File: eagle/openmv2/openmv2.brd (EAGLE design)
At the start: 43.2 x 54.6 mm, 82 parts, among them J3 CON_HEADER_1X03, J4 CON_HEADER_1X03, Q1 MOSFET, U1 TPS2114APW, U10 IS42S16800E, U2 USD-47571, U3 BEAD, U4 TPS768, U5 BEAD, U6 BEAD, U7 STM32F429, U8 VREG_25, U9 OV2640, X1 USB-MICROB

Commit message: Fix SDRAM part-no
* Issue #29
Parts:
- U10: value IS42S16800E -> IS42S81600E-7TL
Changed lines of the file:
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@@
 <layer number="21" name="tPlace" color="7" fill="1" visible="yes" active="yes"/>
 <layer number="22" name="bPlace" color="7" fill="1" visible="yes" active="yes"/>
-<layer number="23" name="tOrigins" color="15" fill="1" visible="no" active="yes"/>
-<layer number="24" name="bOrigins" color="15" fill="1" visible="no" active="yes"/>
+<layer number="23" name="tOrigins" color="15" fill="1" visible="yes" active="yes"/>
+<layer number="24" name="bOrigins" color="15" fill="1" visible="yes" active="yes"/>
 <layer number="25" name="tNames" color="7" fill="1" visible="no" active="yes"/>
 <layer number="26" name="bNames" color="7" fill="1" visible="no" active="yes"/>
@@
 <attribute name="VALUE" x="18.6055" y="32.131" size="0.4064" layer="27"/>
 </element>
-<element name="U10" library="mux" package="TSOPII-54" value="IS42S16800E" x="21.59" y="21.717" smashed="yes" rot="MR270">
+<element name="U10" library="mux" package="TSOPII-54" value="IS42S81600E-7TL" x="21.59" y="21.717" smashed="yes" rot="MR270">
 <attribute name="NAME" x="26.5696" y="9.5388" size="0.6096" layer="26" font="vector" ratio="20" rot="MR0"/>
 <attribute name="VALUE" x="21.8686" y="30.1956" size="1.27" layer="28" rot="MR270"/>

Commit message: Rename Eagle files
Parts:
- removed C12, C21: 100uF, sfe:EIA3216
- removed C25, C26, C27, C28, C29, C31, C32, C35, C36, C37, C43: 0.1uF, sfe:0402-CAP
- removed C30: 10uF, sfe:0805
- removed C33, C34: 2.2uF, sfe:0402-CAP
- removed C38: 100uF, sfe:EIA3528
- removed H1, H8: MOUNT-PAD-ROUND2.8, holes:2,8-PAD
- removed R12: 1K, sfe:0402-RES
- removed R4: 10ohm, iofault:0402-RES
- removed RN2, RN8: (no value), resistor-dil:CAT16
- removed U$1: LENSMOUNT, omnivision:LENSMOUNT
- removed U$14, U$15, U$16, U$17, U$19, U$20: FIDUCIAL, adafruit:FIDUCIAL_1MM
- removed U10: IS42S81600E-7TL, mux:TSOPII-54
- removed U5: BEAD, heka:0402-CAP
- removed X1: USB-MICROB, sfe:USB-MICROB
- added C48, C49: 2.2uF, sfe:0603-CAP
- added D1: BAT54C, diode:SOT23
- added JP3, JP4: (no value), pinhead:1X08
- added JP5, JP6, JP7, JP8: FIDUCIAL1X2, sfe:FIDUCIAL-1X2
- added R2: 10k, sfe:0603-RES
- added U$3: (no value), openmv:OMV-LOGO
- added U12: STM32F427-LQFP100, mux:LQFP100
- added X2: USB-MICROB, sfe:USB-MICROB
- C1: value 0.1uF -> 22uF; device sfe:0402-CAP -> sfe:0805
- C10, C13, C14, C15, C16, C17, C18, C19, C20, C4, C5, C6, C7, C8, C9: device sfe:0402-CAP -> sfe:0603-CAP
- C11: value 100uF -> 22uF; device sfe:EIA3528 -> sfe:0805
- C2: value 0.1uF -> 4.7uF; device sfe:0402-CAP -> sfe:0603-CAP
- C23, C24: value 10uF -> 4.7uF; device sfe:0402-CAP -> sfe:0603-CAP
- C3: device sfe:EIA3216 -> sfe:1206
- C40, C41: value 18pF -> 12pF; device sfe:0402-CAP -> sfe:0603-CAP
- JP1, JP2: value (none) -> FIDUCIAL1X2; device pinhead:1X10 -> sfe:FIDUCIAL-1X2
- LOGO1: value OSHW_LOGO_FILLX0200-NT -> OSHW_LOGO_FILLX0150-NT; device iofault:OSHW_FILLX200_NOTEXT -> iofault:OSHW_FILLX150_NOTEXT
- R1: value 10K -> 10ohm; device sfe:0402-RES -> sfe:0603-RES
- R5: device sfe:0402-RES -> sfe:0603-RES
- RN4: value (none) -> 220R; device resistor-dil:CAT16 -> resistor-dil:EXBV8V
- RN5, RN6: value (none) -> 10K; device resistor-dil:CAT16 -> resistor-dil:EXBV8V
- RN7: value (none) -> 10K
- U1: value TPS2114APW -> LENSMOUNT20MM; device mux:TSSOP8 -> omnivision:LENSMOUNT-20MM
- U3, U6: value BEAD -> (none); device heka:0402-CAP -> sfe:0603
- U4: value TPS768 -> BD33IA; device mux:SOIC8 -> mux:HTSOP-J8
- U7: value STM32F429 -> (none); device stm32:LQFP144 -> sfe:0603
- U8: value VREG_25 -> VREG_28
- Y1: device mux:CRYSTAL3.2X2.5 -> mux:CRYSTAL-2.5X2.0
- moved C3 44.8 mm to (6.22, 2.92), turned to 270 degrees
- moved H2 37.4 mm to (3.30, 41.1)
- moved JP2 34.1 mm to (7.87, 6.10), flipped to the bottom, turned to 0 degrees
- moved U1 32.3 mm to (17.8, 36.0), turned to 0 degrees
- moved H6 30.1 mm to (32.3, 41.1)
- moved C7 27.5 mm to (12.4, 6.48), turned to 180 degrees
- moved C6 25.7 mm to (9.91, 25.0)
- moved C11 23.6 mm to (8.13, 25.0), turned to 270 degrees
- moved R1 23.5 mm to (6.22, 25.0), flipped to the top
- moved C2 23.0 mm to (16.5, 3.30)
- moved C14 22.7 mm to (8.26, 13.7), turned to 270 degrees
- moved R5 19.0 mm to (2.03, 22.2), flipped to the top, turned to 180 degrees
- moved C1 18.9 mm to (27.2, 26.8), turned to 270 degrees
- moved LOGO1 16.7 mm to (26.9, 11.4), flipped to the top
- moved LED3 16.5 mm to (2.41, 35.6), turned to 270 degrees
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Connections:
- removed net ADC12_IN14: JP1.8, U7.44
- removed net ADC12_IN15: JP1.7, U7.45
- removed net ADC12_IN5: U7.41
- removed net DCMI_SCL: RN7.2, U7.69, U9.C2
- removed net DCMI_SDA: RN7.1, U7.70, U9.C1
- removed net DRAM_A0: U10.23, U7.10
- removed net DRAM_A1: U10.24, U7.11
- removed net DRAM_A10: U10.22, U7.56
- removed net DRAM_A11: U10.35, U7.57
- removed net DRAM_A2: U10.25, U7.12
- removed net DRAM_A3: U10.26, U7.13
- removed net DRAM_A4: U10.29, U7.14
- removed net DRAM_A5: U10.30, U7.15
- removed net DRAM_A6: U10.31, U7.50
- removed net DRAM_A7: U10.32, U7.53
- removed net DRAM_A8: U10.33, U7.54
- removed net DRAM_A9: U10.34, U7.55
- removed net DRAM_BA0: U10.20, U7.89
- removed net DRAM_BA1: U10.21, U7.90
- removed net DRAM_CAS: U10.17, U7.132
- removed net DRAM_CLK: U10.38, U7.93
- removed net DRAM_CLKE: U10.37, U7.29
- removed net DRAM_CS: R1.2, U10.19, U7.28
- removed net DRAM_D0: U10.2, U7.85
- removed net DRAM_D1: U10.5, U7.86
- removed net DRAM_D2: U10.8, U7.114
- removed net DRAM_D3: U10.11, U7.115
- removed net DRAM_D4: U10.44, U7.58
- removed net DRAM_D5: U10.47, U7.59
- removed net DRAM_D6: U10.50, U7.60
- removed net DRAM_D7: U10.53, U7.63
- removed net DRAM_DQM: U10.39, U7.141
- removed net DRAM_RAS: U10.18, U7.49
- removed net DRAM_WE: U10.16, U7.26
- removed net FS_DN: U7.103, X1.D-
- removed net N$15: U7.128
- removed net N$17: U7.92
- removed net N$18: U7.18
- removed net N$19: U7.91
- removed net N$20: JP1.1, RN8.1
- removed net N$21: JP1.2, RN8.2
- removed net N$22: U5.1, X1.VBUS
- removed net N$23: JP1.3, RN8.3
- removed net N$24: JP1.4, RN8.4
- removed net N$25: U7.122
- removed net N$26: R12.2, U1.4
- removed net N$27: U7.19
- removed net N$28: U7.20
- removed net SPI4_MISO: RN8.6, U7.4
- removed net SPI4_MOSI: RN8.5, U7.5
- removed net SPI4_NSS: RN8.7, U7.2
- removed net SPI4_SCK: RN8.8, U7.1
- removed net TIM12_CH1: U7.75
- removed net TIM12_CH2: U7.76
- removed net USART2_RX: JP1.6, U7.37
- removed net USART2_TX: JP1.5, U7.36
- removed net USART3_RX: JP2.7, U7.78
- removed net USART3_TX: JP2.8, U7.77
- removed net VBAT: J3.2, J4.2, JP2.9, U1.6
- new net DAC: JP4.7, U12.30
- new net EXPST: U12.55, U9.A2
- new net FREX: U12.56, U9.B2
- new net FS_DM: U12.70, X2.D-
- new net I2C1_SCL: RN7.2, U12.95, U9.C2
- new net I2C1_SDA: RN7.1, U12.96, U9.C1
- new net I2C2_SCL: JP4.5, U12.47
- new net I2C2_SDA: JP4.6, U12.48
- new net RAW: D1.1, J3.2, J4.2, JP3.7
- new net SPI2_MISO: JP4.2, U12.53
- new net SPI2_MOSI: JP4.1, U12.54
- new net SPI2_NSS: JP4.4, U12.51
- new net SPI2_SCLK: JP4.3, U12.52
- new net STROBE: U12.84, U9.A6
- net BOOT0: now also JP3.3, RN5.8, U12.94; no longer JP2.3, RN2.6, U7.138
- net DCMI_CLK: now also U12.67; no longer U7.100
- net DCMI_D0: now also U12.63; no longer U7.96
- net DCMI_D1: now also U12.64; no longer U7.97
- net DCMI_D2: now also U12.97; no longer U7.125
- net DCMI_D3: now also U12.98; no longer U7.126
- net DCMI_D4: now also U12.3; no longer U7.3
- net DCMI_D5: now also U12.92; no longer U7.117
- net DCMI_D6: now also U12.4; no longer U7.139
- net DCMI_D7: now also U12.5; no longer U7.140
- net DCMI_HSYNC: now also U12.29; no longer U7.40
- net DCMI_PCLK: now also U12.31; no longer U7.42
- net DCMI_PWDN: now also U12.91; no longer U7.102
- net DCMI_RST: now also U12.69; no longer U7.110
- net DCMI_VSYNC: now also U12.93; no longer U7.137
- net FS_DP: now also U12.71, X2.D+; no longer U7.104, X1.D+
- net GND: now also C11.1, C3.2, C48.2, C49.2, JP3.8, R2.1, RN5.1, U12.10, U12.20, U12.27, U12.37, U12.74, U12.99, U4.3, U4.P$1, X2.GND; no longer C11.C, C12.C, C21.C, C25.2, C26.2, C27.2, C28.1, C29.2, C3.C, C30.2, C31.2, C32.2, C33.2, C34.2, C35.2, C36.2, C37.2, C38.C, C43.2, H1.B2,8, H2.B2,8, H6.B2,8, H8.B2,8, JP1.10, JP2.10, R12.1, RN2.1, RN2.3, U$1.P$1, U$1.P$2, U1.3, U1.5, U10.12, U10.28, U10.41, U10.46, U10.52, U10.54, U10.6, U4.1, U4.2, U7.107, U7.120, U7.130, U7.16, U7.31, U7.38, U7.48, U7.51, U7.61, U7.83, U7.94, U9.A2, U9.B2, X1.GND
- net LED_B: now also U12.16; no longer U7.135
- net LED_G: now also U12.17; no longer U7.136
- net LED_IR: now also U12.1; no longer U7.133
- net LED_R: now also U12.15; no longer U7.134
- net N$10: now also R1.2; no longer R4.1
- net N$12: now also C4.1, C5.1, U12.21, U12.22, U3.1; no longer U7.127
- net N$14: now also R1.1; no longer R4.2
- net N$2: now also U12.13; no longer U7.23
- net N$4: now also U12.12; no longer U7.24
- net N$5: now also R2.2
- net N$7: now also U7.1, X2.VBUS; no longer C4.1, C5.1, U3.1, U7.32, U7.33
- net NRST: now also JP3.4, RN5.7, U12.14; no longer JP2.4, RN2.5, U7.25
- net SDIO_CLK: now also U12.80; no longer U7.113
- net SDIO_CMD: now also U12.83; no longer U7.116
- net SDIO_D0: now also RN5.6, U12.65; no longer RN5.7, U7.98
- net SDIO_D1: now also U12.66; no longer U7.99
- net SDIO_D2: now also U12.78; no longer U7.111
- net SDIO_D3: now also U12.79; no longer U7.112
- net SD_CD: now also U12.77; no longer U7.124
- net SWCLK: now also JP3.1, U12.76; no longer JP2.1, RN2.8, U7.109
- net SWDIO: now also JP3.2, U12.72; no longer JP2.2, RN2.7, U7.105
- net TIM4_CH1: now also JP3.6, U12.59; no longer JP2.6, U7.81
- net TIM4_CH2: now also JP3.5, U12.60; no longer JP2.5, U7.82
- net VBUS: now also D1.2, U12.68, U7.2; no longer C43.1, U1.8, U5.2, U7.101
- net VCAP1: now also C49.1, U12.49; no longer C34.1, U7.71
- net VCAP2: now also C48.1, U12.73; no longer C33.1, U7.106
- net VCC: now also C11.2, C3.1, JP4.8, U12.100, U12.11, U12.19, U12.28, U12.50, U12.6, U12.75, U4.1, U4.2; no longer C12.A, C2.1, C21.A, C25.1, C26.1, C27.1, C28.2, C29.1, C3.A, C30.1, C31.1, C32.1, C35.1, C36.1, C37.1, C38.A, JP1.9, R1.1, RN2.2, RN2.4, RN5.1, U10.1, U10.14, U10.27, U10.3, U10.43, U10.49, U10.9, U4.5, U4.6, U7.108, U7.121, U7.131, U7.143, U7.144, U7.17, U7.30, U7.39, U7.52, U7.6, U7.62, U7.72, U7.84, U7.95
- net VIN: now also C2.1, D1.3, U4.5, U4.8; no longer C11.A, U1.7, U4.3, U4.4
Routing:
- net VCC: track 102.3 -> 26.3 mm, vias 32 -> 33
- net GND: track 123.5 -> 53.8 mm, vias 319 -> 61
- net DCMI_SCL: track 46.4 -> 0.00 mm, vias 4 -> 0
- net DCMI_SDA: track 43.5 -> 0.00 mm, vias 4 -> 0
- net EXPST: track 0.00 -> 39.3 mm, vias 0 -> 2
- net FREX: track 0.00 -> 37.3 mm, vias 0 -> 2
- net SPI2_SCLK: track 0.00 -> 30.5 mm
- net VBAT: track 30.2 -> 0.00 mm, vias 1 -> 0
- net SPI2_MOSI: track 0.00 -> 30.0 mm, vias 0 -> 1
- net SPI2_NSS: track 0.00 -> 28.8 mm
- net SPI2_MISO: track 0.00 -> 28.4 mm, vias 0 -> 1
- net FS_DN: track 26.3 -> 0.00 mm
- net DRAM_D7: track 25.8 -> 0.00 mm, vias 1 -> 0
- net I2C2_SDA: track 0.00 -> 25.7 mm, vias 0 -> 1
- net RAW: track 0.00 -> 24.1 mm, vias 0 -> 4
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- added copper zone on layer 1, net N$12
- added copper zone on layer 1, net N$7
- added copper zone on layer 1, net RAW
- added copper zone on layer 16, net RAW
- added copper zone on layer 1, net VBUS
- added copper zone on layer 1, net VCC
- added copper zone on layer 1, net VIN
- removed copper zone on layer 16, net GND
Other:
- board size 43.2 x 54.6 mm -> 35.6 x 44.5 mm
- board text added: "DAC"
- board text added: "MISO"
- board text added: "MOSI"
- board text added: "VCC"
- board text added: "VOUT"
- board text removed: "3.3v"
- board text removed: "ADC1"
- board text removed: "ADC2"
- board text removed: "OpenMV2 R1"
- board text removed: "SDI"
- board text removed: "SDO"
- board text removed: "VIN"
- board text removed: "penMV"

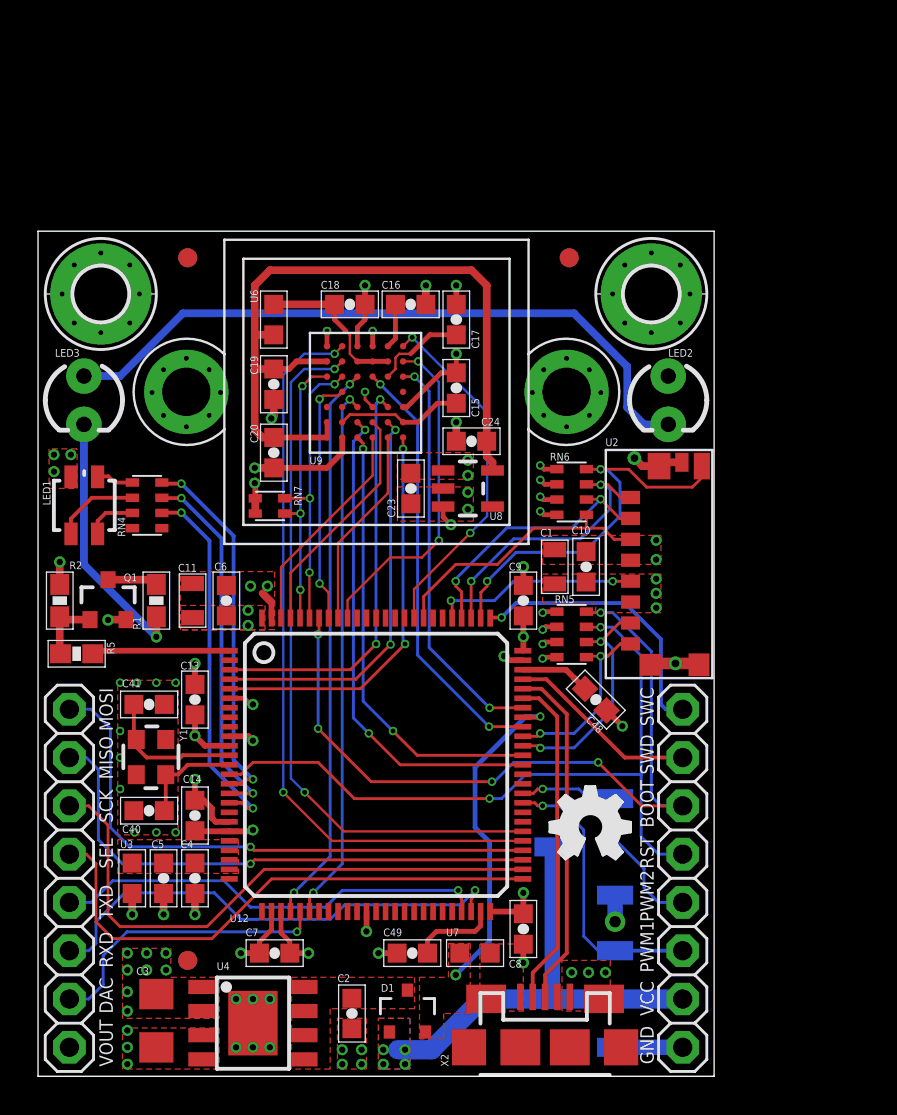
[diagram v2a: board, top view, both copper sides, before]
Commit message: Update Eagle files.
* Add OpenMV2-R5
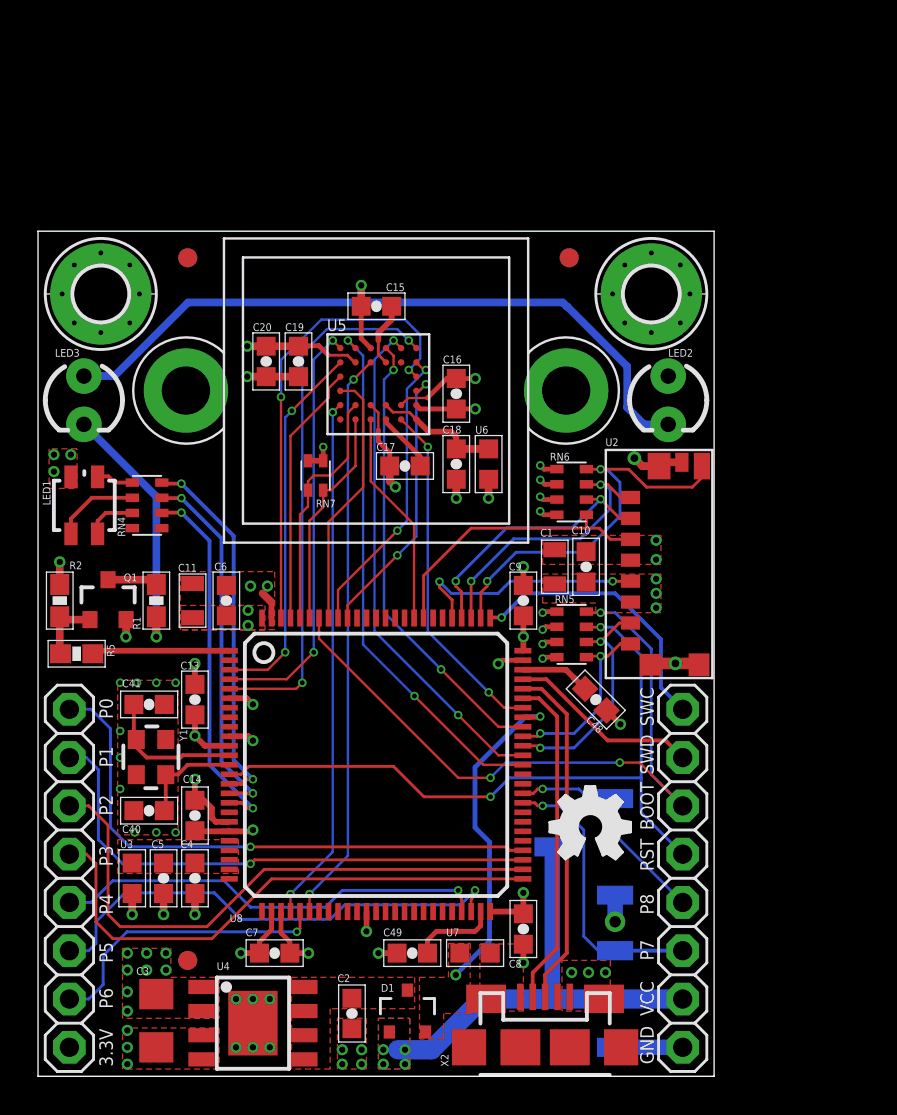
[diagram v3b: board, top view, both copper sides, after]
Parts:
- removed C23, C24: 4.7uF, sfe:0603-CAP
- removed U12: STM32F427-LQFP100, mux:LQFP100
- removed U9: OV2640, omnivision:CSP2
- added U5: OV7725, omnivision:CSP2-28
- C15, C19: value 4.7uF -> 0.1uF
- C20: value 0.1uF -> 4.7uF
- U8: value VREG_28 -> STM32F427-LQFP100; device sfe:SOT23-5 -> mux:LQFP100
- moved U8 15.3 mm to (17.8, 16.4), turned to 0 degrees
- moved U6 13.6 mm to (23.7, 32.2)
- moved C18 10.1 mm to (22.0, 32.2), turned to 270 degrees
- moved C17 8.16 mm to (19.3, 32.1), turned to 180 degrees
- moved C15 6.01 mm to (17.8, 40.5), turned to 180 degrees
- moved C16 5.28 mm to (22.0, 35.9), turned to 270 degrees
- moved C20 4.82 mm to (12.0, 37.6)
- moved RN7 2.88 mm to (14.6, 31.6), turned to 0 degrees
- moved C19 1.77 mm to (13.7, 37.6)
- moved U1 0.07 mm to (17.8, 36.1)
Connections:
- removed net 2.8V: C19.1, C20.1, C24.1, U6.2, U8.5, U9.B1, U9.F1, U9.G1
- removed net N$6: C15.1, U9.F2, U9.F6
- removed net STROBE: U12.84, U9.A6
- new net FSIN: U5.A4, U8.84
- new net N$15: C15.1, U5.E3
- net BOOT0: now also U8.94; no longer U12.94
- net DAC: now also U8.30; no longer U12.30
- net DCMI_CLK: now also U5.F3, U8.67; no longer U12.67, U9.C4
- net DCMI_D0: now also U5.F5, U8.63; no longer U12.63, U9.F3
- net DCMI_D1: now also U5.F2, U8.64; no longer U12.64, U9.G3
- net DCMI_D2: now also U5.D6, U8.97; no longer U12.97, U9.F4
- net DCMI_D3: now also U5.D1, U8.98; no longer U12.98, U9.G4
- net DCMI_D4: now also U5.E6, U8.3; no longer U12.3, U9.E5
- net DCMI_D5: now also U5.E1, U8.92; no longer U12.92, U9.G5
- net DCMI_D6: now also U5.F6, U8.4; no longer U12.4, U9.F5
- net DCMI_D7: now also U5.F1, U8.5; no longer U12.5, U9.G6
- net DCMI_HSYNC: now also U5.B6, U8.29; no longer U12.29, U9.C3
- net DCMI_PCLK: now also U5.E4, U8.31; no longer U12.31, U9.E3
- net DCMI_PWDN: now also U5.C1, U8.91; no longer U12.91, U9.B6
- net DCMI_RST: now also U5.A2, U8.69; no longer U12.69, U9.C6
- net DCMI_VSYNC: now also U5.C6, U8.93; no longer U12.93, U9.D2
- net EXPST: now also U8.55; no longer U12.55, U9.A2
- net FREX: now also U8.56; no longer U12.56, U9.B2
- net FS_DM: now also U8.70; no longer U12.70
- net FS_DP: now also U8.71; no longer U12.71
- net GND: now also U5.B1, U5.B4, U5.F4, U8.10, U8.20, U8.27, U8.37, U8.74, U8.99; no longer C23.2, C24.2, U12.10, U12.20, U12.27, U12.37, U12.74, U12.99, U8.2, U9.A1, U9.A3, U9.A4, U9.E4, U9.E6, U9.G2
- net I2C1_SCL: now also U5.A5, U8.95; no longer U12.95, U9.C2
- net I2C1_SDA: now also U5.B5, U8.96; no longer U12.96, U9.C1
- net I2C2_SCL: now also U8.47; no longer U12.47
- net I2C2_SDA: now also U8.48; no longer U12.48
- net LED_B: now also U8.16; no longer U12.16
- net LED_G: now also U8.17; no longer U12.17
- net LED_IR: now also U8.1; no longer U12.1
- net LED_R: now also U8.15; no longer U12.15
- net N$1: now also U5.A3; no longer U9.C5
- net N$12: now also U8.21, U8.22; no longer U12.21, U12.22
- net N$13: now also U5.A1, U5.B3; no longer U9.B3, U9.B4, U9.B5
- net N$2: now also U8.13; no longer U12.13
- net N$3: now also U5.B2; no longer U9.A5
- net N$4: now also U8.12; no longer U12.12
- net NRST: now also U8.14; no longer U12.14
- net SDIO_CLK: now also U8.80; no longer U12.80
- net SDIO_CMD: now also U8.83; no longer U12.83
- net SDIO_D0: now also U8.65; no longer U12.65
- net SDIO_D1: now also U8.66; no longer U12.66
- net SDIO_D2: now also U8.78; no longer U12.78
- net SDIO_D3: now also U8.79; no longer U12.79
- net SD_CD: now also U8.77; no longer U12.77
- net SPI2_MISO: now also U8.53; no longer U12.53
- net SPI2_MOSI: now also U8.54; no longer U12.54
- net SPI2_NSS: now also U8.51; no longer U12.51
- net SPI2_SCLK: now also U8.52; no longer U12.52
- net SWCLK: now also U8.76; no longer U12.76
- net SWDIO: now also U8.72; no longer U12.72
- net TIM4_CH1: now also U8.59; no longer U12.59
- net TIM4_CH2: now also U8.60; no longer U12.60
- net VBUS: now also U8.68; no longer U12.68
- net VCAP1: now also U8.49; no longer U12.49
- net VCAP2: now also U8.73; no longer U12.73
- net VCC: now also C19.1, C20.1, U5.E5, U6.2, U8.100, U8.11, U8.19, U8.28, U8.50, U8.6, U8.75; no longer C23.1, U12.100, U12.11, U12.19, U12.28, U12.50, U12.6, U12.75, U8.1, U8.3
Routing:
- net 2.8V: track 40.1 -> 0.00 mm
- net EXPST: track 39.3 -> 0.00 mm, vias 2 -> 0
- net FREX: track 37.3 -> 0.00 mm, vias 2 -> 0
- net STROBE: track 18.7 -> 0.00 mm, vias 2 -> 0
- net DCMI_D3: track 11.5 -> 24.8 mm, vias 0 -> 2
- net FSIN: track 0.00 -> 11.4 mm
- net DCMI_D7: track 21.1 -> 28.3 mm
- net N$6: track 6.75 -> 0.00 mm, vias 0 -> 1
- net VCC: track 26.3 -> 32.3 mm, vias 33 -> 32
- net DCMI_D5: track 10.6 -> 15.6 mm, vias 0 -> 2
- net GND: track 53.8 -> 48.8 mm, vias 61 -> 54
- net BOOT0: track 41.3 -> 37.7 mm, vias 5 -> 3
- net I2C1_SCL: track 15.2 -> 11.7 mm, vias 3 -> 0
- net N$15: track 0.00 -> 3.41 mm, vias 1 -> 0
- net DCMI_PWDN: track 17.7 -> 14.6 mm
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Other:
- board text added: "3.3V"
- board text added: "P0"
- board text added: "P1"
- board text added: "P2"
- board text added: "P3"
- board text added: "P4"
- board text added: "P5"
- board text added: "P6"
- board text added: "P7"
- board text added: "P8"
- board text removed: "DAC"
- board text removed: "MISO"
- board text removed: "MOSI"
- board text removed: "PWM1"
- board text removed: "PWM2"
- board text removed: "RXD"
- board text removed: "SCK"
- board text removed: "SEL"
- board text removed: "TXD"
- board text removed: "VOUT"

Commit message: Update silkscreen
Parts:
- added U$1: (no value), openmv:WEEE
- added U$2: (no value), openmv:ROHS
- added U$4: (no value), openmv:OMV-LOGO-SMALL
- moved U$3 38.0 mm to (24.0, 39.0)
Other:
- board text added: "2/9/2016"
- board text added: "Built by MacroFab"
- board text added: "LED1=Red"
- board text added: "LED2=Green"
- board text added: "LED3=Blue"
- board text added: "LED4=IR"
- board text added: "Made in USA"
- board text added: "OV7725 - Rev 1"
- board text added: "OpenMV Cam 2"
- board text added: "P0=PB15/MOSI"
- board text added: "P1=PB14/MISO"
- board text added: "P2=PB13/SCLK"
- board text added: "P3=PB12/SS"
- board text added: "P4=PB10/TXD/SCL"
- board text added: "P5=PB11/RXD/SDA"
- board text added: "P6=PA5/ADC/DAC"
- board text added: "P7=PD12/SERVO1"
- board text added: "P8=PD13/SERVO2"
- board text added: "Pin List"
- board text added: "VIN"
- board text added: "https://openmv.io"
